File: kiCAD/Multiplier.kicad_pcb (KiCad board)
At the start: 2 copper layers, 55 parts, among them IC2 ADG1221BRMZ, J1 Conn_01x02_Pin, J2 Conn_01x02_Pin, J3 Conn_01x01_Pin, Q1 BC846BPN, Q2 BC846BPN, U1 TS912, U10 TPS63060, U2 LM339, U4 TS912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

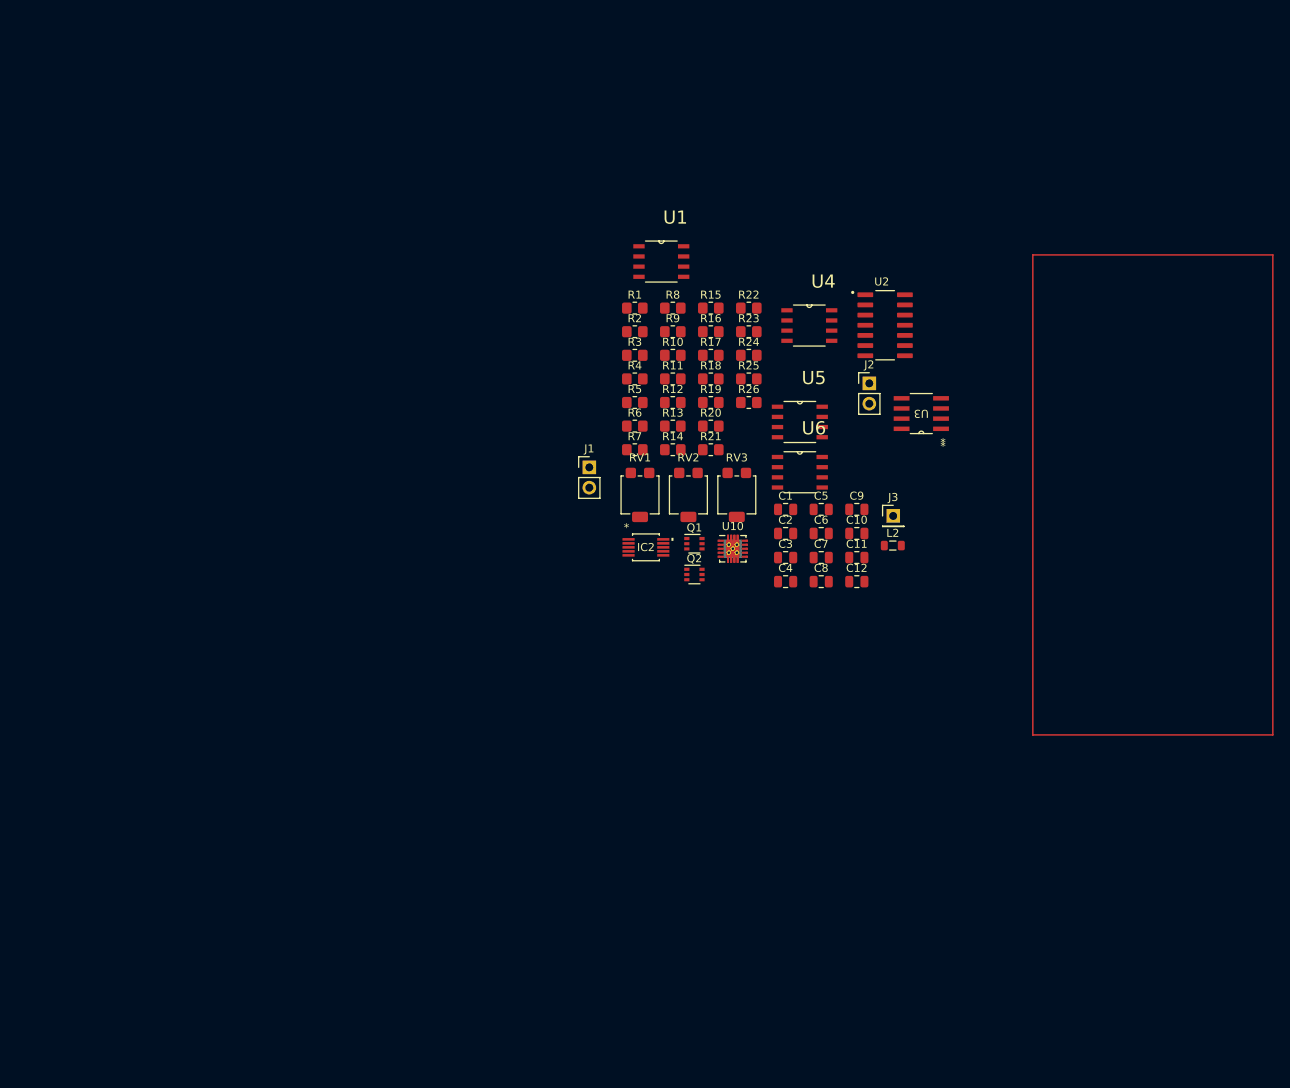
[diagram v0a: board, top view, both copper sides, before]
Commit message: Replacing schematics for TLV3402IDR assigning footpritns and adding first PCB layout
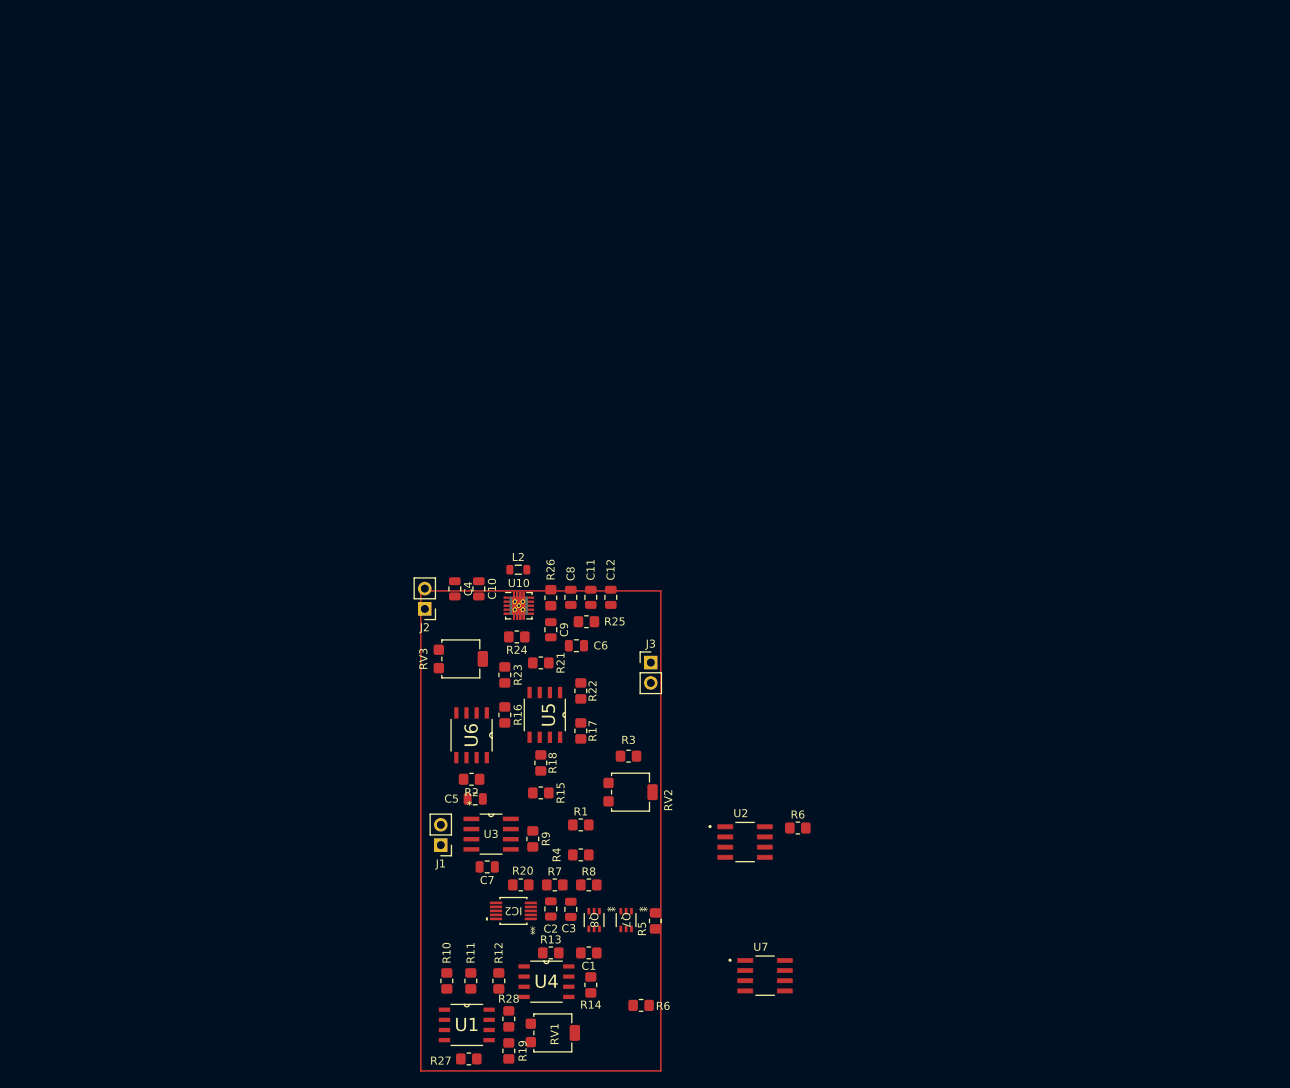
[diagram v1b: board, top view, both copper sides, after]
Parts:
- removed Q1, Q2: BC846BPN, Package_TO_SOT_SMD:SOT-363_SC-70-6
- removed the R6 at (135.2, 68.9)
- added Q7: Q_Dual_PNP_PNP_C1B1B2C2E2E1, Custom:SOT-363_DUAL_PNP, F.Cu at (134.2, 130.6)
- added Q8: Q_Dual_PNP_PNP_C1B1B2C2E2E1, Custom:SOT-363_DUAL_PNP, F.Cu at (130.2, 130.6)
- added R27: 10k, Resistor_SMD:R_0805_2012Metric_Pad1.20x1.40mm_HandSolder, F.Cu at (114.5, 148.0)
- added R28: 10k, Resistor_SMD:R_0805_2012Metric_Pad1.20x1.40mm_HandSolder, F.Cu at (119.5, 143.0)
- added R6: 10k, Resistor_SMD:R_0805_2012Metric_Pad1.20x1.40mm_HandSolder, F.Cu at (155.6, 119.1)
- added R6: 10k, Resistor_SMD:R_0805_2012Metric_Pad1.20x1.40mm_HandSolder, F.Cu at (136.0, 141.3)
- added U7: TLV340, Custom:TLV3402IDR_SOIC8, F.Cu at (151.5, 137.6)
- C1: footprint Capacitor_SMD:C_0805_2012Metric -> Resistor_SMD:R_0805_2012Metric_Pad1.20x1.40mm_HandSolder
- J3: value Conn_01x01_Pin -> Conn_01x02_Pin; footprint Connector_PinHeader_2.54mm:PinHeader_1x01_P2.54mm_Vertical -> Connector_PinHeader_2.54mm:PinHeader_1x02_P2.54mm_Vertical
- U2: value LM339 -> TLV340; footprint Custom:LM339_SOIC14 -> Custom:TLV3402IDR_SOIC8
- moved U1 98.5 mm to (114.2, 143.8)
- moved U4 88.4 mm to (124.2, 138.3)
- moved R19 84.9 mm to (119.5, 147.0), turned to 90 degrees
- moved R10 83.1 mm to (111.8, 138.2), turned to -90 degrees
- moved R11 79.4 mm to (114.8, 138.2), turned to 90 degrees
- moved R12 75.5 mm to (118.2, 138.2), turned to 90 degrees
- moved U3 75.2 mm to (117.3, 119.9), turned to 0 degrees
- moved R8 72.9 mm to (129.5, 126.2)
- moved RV1 68.1 mm to (125.0, 144.8), turned to 90 degrees
- moved R14 67.7 mm to (129.8, 138.8), turned to 90 degrees
- moved R13 67.6 mm to (124.8, 134.8)
- moved U2 66.9 mm to (149.0, 120.9)
- moved R9 65.8 mm to (122.5, 120.5), turned to -90 degrees
- moved R1 65.0 mm to (128.5, 118.8)
- moved R5 64.9 mm to (137.8, 130.8), turned to 90 degrees
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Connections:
- net IN1 renamed PWM_OUT
- C1 pad 1: Net-(Q1B-C2) -> Net-(Q8B-C2)
- J3 pad 1: UxUy -> GND
- R1 pad 2: Net-(U2A-+) -> Net-(U7A-+)
- R10 pad 1: Net-(U1A--) -> Net-(R10-Pad1)
- R11 pad 1: Net-(U1B--) -> Net-(R11-Pad1)
- R3 pad 1: Net-(U2A--) -> Net-(U2B-+)
- R4 pad 2: Net-(U2A--) -> Net-(U2B-+)
- RV2 pad 1: Net-(U2A-+) -> Net-(U7A-+)
- RV2 pad 2: Net-(U2A--) -> Net-(U2B-+)
- U1 pad 1: Net-(U1A--) -> Net-(R10-Pad1)
- U1 pad 7: Net-(U1B--) -> Net-(R11-Pad1)
- U2 pad 2: Net-(Q1B-C2) -> Net-(Q8B-C2)
- U2 pad 3: VCC -> Ux+Er
- U2 pad 4: Net-(U2A--) -> GND
- U2 pad 5: Net-(U2A-+) -> Net-(U2B-+)
- U2 pad 6: Net-(Q1B-C2) -> Net-(Q8B-C2)
- U2 pad 7: Ux+Er -> Net-(U7A-+)
- U2 pad 8: (no net) -> VCC

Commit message: New footprint for buck-boost converter
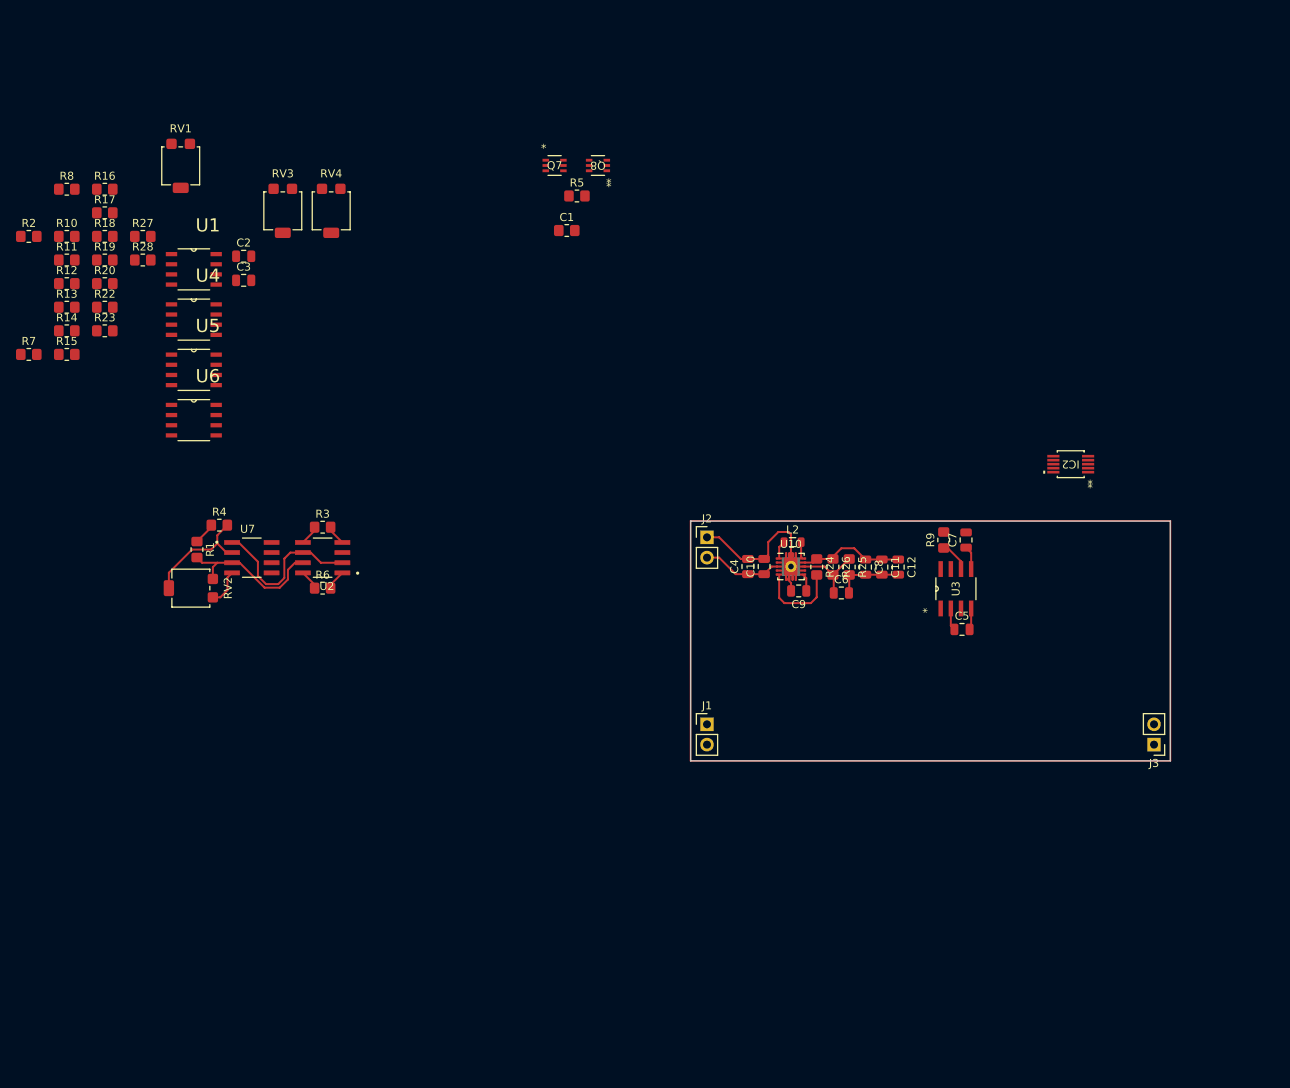
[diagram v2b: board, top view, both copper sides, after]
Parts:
- removed R21: 4k, Resistor_SMD:R_0805_2012Metric_Pad1.20x1.40mm_HandSolder
- removed the R6 at (155.6, 119.1)
- removed the R6 at (136.0, 141.3)
- added R6: 10k, Resistor_SMD:R_0805_2012Metric_Pad1.20x1.40mm_HandSolder, F.Cu at (96.2, 89.2)
- added RV4: 3k, Potentiometer_SMD:Potentiometer_Bourns_3314G_Vertical, F.Cu at (97.3, 42.0)
- R22: value 3k -> 7,5k
- R3: value 25k -> 24k
- RV1: value 1,1k -> 1,15k
- RV2: value 12k -> 12,5k
- RV3: value 1,1k -> 2,4k
- U10: footprint Package_SON:Texas_S-PWSON-N10_ThermalVias -> Custom:Texas_S-PWSON-N10_ThermalVias_Custom
- moved RV1 117.9 mm to (78.5, 36.4), turned to 0 degrees
- moved R19 111.0 mm to (69.0, 48.1), turned to 0 degrees
- moved R27 110.6 mm to (73.7, 45.2)
- moved R8 108.7 mm to (64.2, 39.3)
- moved R28 105.3 mm to (73.7, 48.1), turned to 0 degrees
- moved R14 104.8 mm to (64.2, 57.0), turned to 0 degrees
- moved R10 104.5 mm to (64.2, 45.2), turned to 0 degrees
- moved R11 103.3 mm to (64.2, 48.1), turned to 0 degrees
- moved R12 102.5 mm to (64.2, 51.1), turned to 0 degrees
- moved R13 100.9 mm to (64.2, 54.0)
- moved U1 100.4 mm to (80.1, 49.3)
- moved Q7 94.7 mm to (125.2, 36.3), turned to 0 degrees
- moved Q8 94.3 mm to (130.6, 36.3), turned to 180 degrees
- moved U4 93.8 mm to (80.1, 55.6)
- moved R7 93.4 mm to (59.5, 59.9)
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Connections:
- R22 pad 2: Net-(U5A--) -> Net-(R22-Pad2)
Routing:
- net GND: track 0.00 -> 35.7 mm
- net Net-(Q8B-C2): track 0.00 -> 20.6 mm
- net Net-(U7A-+): track 0.00 -> 19.1 mm
- net VCC: track 0.00 -> 18.5 mm
- net Net-(U2B-+): track 0.00 -> 17.4 mm
- net Net-(U10-PG): track 0.00 -> 11.0 mm
- net VBUS: track 0.00 -> 10.3 mm
- net Net-(U10-FB): track 0.00 -> 9.36 mm
- net Net-(U3-LV): track 0.00 -> 4.01 mm
- net Vcc-: track 0.00 -> 2.95 mm
- net Net-(U3-CAP+): track 0.00 -> 2.80 mm
- net Net-(U3-CAP-): track 0.00 -> 2.70 mm
- net PWM_OUT: track 0.00 -> 2.51 mm
- net Net-(U10-L1): track 0.00 -> 2.30 mm
- net Net-(U10-VAUX): track 0.00 -> 2.23 mm
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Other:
- board outline added: 59.9 x 30 mm

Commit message: Initial routing and layout
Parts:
- moved R14 124.4 mm to (186.2, 32.3)
- moved R20 116.7 mm to (175.5, 98.8)
- moved R13 114.9 mm to (177.8, 36.3)
- moved R12 107.8 mm to (169.9, 29.7)
- moved U4 101.5 mm to (177.8, 27.9)
- moved R10 96.5 mm to (157.5, 20.3)
- moved R11 91.3 mm to (153.2, 27.3)
- moved R19 86.7 mm to (155.7, 48.5)
- moved RV1 84.8 mm to (162.1, 50.5)
- moved U1 84.0 mm to (161.3, 27.8)
- moved R27 80.2 mm to (152.9, 32.5)
- moved R28 80.2 mm to (152.9, 35.6)
- moved R7 70.7 mm to (124.7, 32.8)
- moved R15 64.1 mm to (128.3, 63.5)
- moved Q8 60.6 mm to (98.0, 87.4)
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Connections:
- C1 pad 1: Net-(Q8B-C2) -> Net-(Q7B-C2)
- Q7 pad 3: Net-(Q7A-E1) -> Net-(Q7A-B1)
- Q7 pad 5: VCC -> Net-(Q7B-E2)
- Q8 pad 3: Net-(Q7A-B1) -> Net-(Q7A-E1)
- Q8 pad 4: Net-(Q8B-C2) -> Net-(Q7B-E2)
- Q8 pad 5: Net-(Q7B-C2) -> VCC
- U2 pad 2: Net-(Q8B-C2) -> Net-(Q7B-C2)
- U2 pad 6: Net-(Q8B-C2) -> Net-(Q7B-C2)
- U7 pad 1: Net-(Q8B-C2) -> Net-(Q7B-C2)
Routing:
- net Net-(Q7B-C2): track 0.00 -> 33.2 mm
- net Net-(Q8B-C2): track 20.6 -> 0.00 mm
- net Net-(Q7B-E2): track 0.00 -> 5.28 mm
- net Net-(Q7A-B1): track 0.00 -> 4.25 mm
- net Net-(Q7A-E1): track 0.00 -> 4.21 mm
- net VCC: track 18.5 -> 19.1 mm
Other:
- board text added: "Adder"
- board text added: "Buffered Er Ux"
- board text added: "ER voltage div"
- board text added: "RMS"
- board text added: "curr_mirr"
- board text added: "one quadrant mul"
- board text added: "suctractor"
